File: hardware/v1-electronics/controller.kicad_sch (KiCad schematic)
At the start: 15 parts, among them J3 Female JST-SH, SW8 SW_Push, U1 MDBT50Q-1MV2

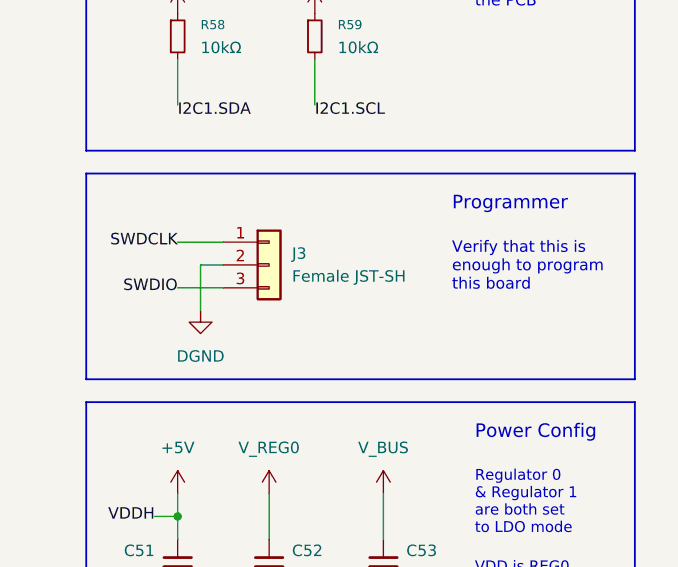
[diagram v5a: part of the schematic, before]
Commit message: feat(v1 hardware): aligned schematic symbols with pcb footprints
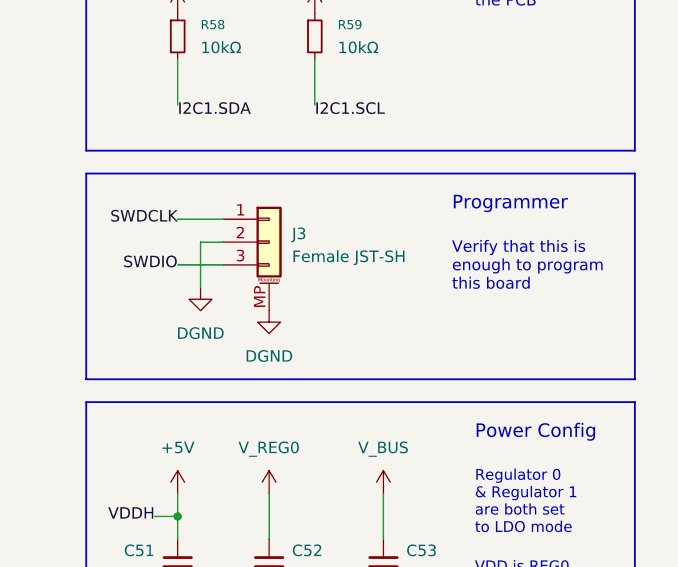
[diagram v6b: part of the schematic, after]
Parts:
- J3: symbol Connector_Generic:Conn_01x03 -> Connector_Generic_MountingPin:Conn_01x03_MountingPin
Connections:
- net DGND: now also J3.MP (MountPin)
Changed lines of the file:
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@@
 	(wire
 		(pts
-			(xy 25.4 76.2) (xy 30.48 76.2)
+			(xy 25.4 73.66) (xy 30.48 73.66)
 		)
 		(stroke
@@
 	(wire
 		(pts
-			(xy 27.94 78.74) (xy 27.94 73.66)
+			(xy 27.94 76.2) (xy 27.94 71.12)
 		)
 		(stroke
@@
 	(wire
 		(pts
-			(xy 27.94 73.66) (xy 30.48 73.66)
+			(xy 27.94 71.12) (xy 30.48 71.12)
 		)
 		(stroke
@@
 	(wire
 		(pts
-			(xy 25.4 71.12) (xy 30.48 71.12)
+			(xy 25.4 68.58) (xy 30.48 68.58)
 		)
 		(stroke
@@
 	)
 	(label "SWDCLK"
-		(at 25.4 71.12 180)
+		(at 25.4 68.58 180)
 		(effects
 			(font
@@
 	)
 	(label "SWDIO"
-		(at 25.4 76.2 180)
+		(at 25.4 73.66 180)
 		(effects
 			(font
@@
 	(symbol
 		(lib_id "power:GND")
-		(at 27.94 78.74 0)
+		(at 27.94 76.2 0)
 		(unit 1)
 		(body_style 1)
@@
 		(dnp no)
 		(property "Reference" "#PWR0123"
-			(at 27.94 85.09 0)
+			(at 27.94 82.55 0)
 			(hide yes)
 			(show_name no)
@@
 		)
 		(property "Value" "DGND"
-			(at 27.94 83.82 0)
+			(at 27.94 81.28 0)
 			(show_name no)
 			(do_not_autoplace no)
@@
 		)
 		(property "Footprint" ""
-			(at 27.94 78.74 0)
+			(at 27.94 76.2 0)
 			(hide yes)
 			(show_name no)
@@
 		)
 		(property "Datasheet" ""
-			(at 27.94 78.74 0)
+			(at 27.94 76.2 0)
 			(hide yes)
 			(show_name no)
@@
 		)
 		(property "Description" "Power symbol creates a global label with name \"GND\" , ground"
-			(at 27.94 78.74 0)
+			(at 27.94 76.2 0)
 			(hide yes)
 			(show_name no)
@@
 	)
 	(symbol
+		(lib_id "power:GND")
+		(at 35.56 78.74 0)
+		(unit 1)
+		(body_style 1)
+		(exclude_from_sim no)
+		(in_bom yes)
+		(on_board yes)
+		(in_pos_files yes)
+		(dnp no)
+		(property "Reference" "#PWR0156"
+			(at 35.56 85.09 0)
+			(hide yes)
+			(show_name no)
+			(do_not_autoplace no)
+			(effects
+				(font
+					(size 1.27 1.27)
+				)
+			)
+		)
+		(property "Value" "DGND"
+			(at 35.56 83.82 0)
+			(show_name no)
+			(do_not_autoplace no)
+			(effects
+				(font
+					(size 1.27 1.27)
+				)
+			)
+		)
+		(property "Footprint" ""
+			(at 35.56 78.74 0)
+			(hide yes)
+			(show_name no)
+			(do_not_autoplace no)
+			(effects
+				(font
+					(size 1.27 1.27)
+				)
+			)
+		)
+		(property "Datasheet" ""
+			(at 35.56 78.74 0)
+			(hide yes)
+			(show_name no)
+			(do_not_autoplace no)
+			(effects
+				(font
+					(size 1.27 1.27)
+				)
+			)
+		)
+		(property "Description" "Power symbol creates a global label with name \"GND\" , ground"
+			(at 35.56 78.74 0)
+			(hide yes)
+			(show_name no)
+			(do_not_autoplace no)
+			(effects
+				(font
+					(size 1.27 1.27)
+				)
+			)
+		)
+		(pin "1"
+		)
+		(instances
+			(project "slack"
+				(path "/504df67f-9f45-483f-90c8-f14c049b6b02/af928721-79e0-4dbd-9302-cd57a57ce5a4"
+					(reference "#PWR0156")
+					(unit 1)
+				)
+			)
+		)
+	)
+	(symbol
 		(lib_id "Device:R_Small")
 		(at 40.64 48.26 0)
@@
 	)
 	(symbol
-		(lib_id "Connector_Generic:Conn_01x03")
-		(at 35.56 73.66 0)
+		(lib_id "Connector_Generic_MountingPin:Conn_01x03_MountingPin")
+		(at 35.56 71.12 0)
 		(unit 1)
 		(body_style 1)
@@
 		(fields_autoplaced yes)
 		(property "Reference" "J3"
-			(at 38.1 72.3899 0)
+			(at 38.1 70.2055 0)
 			(show_name no)
 			(do_not_autoplace no)
@@
 		)
 		(property "Value" "Female JST-SH"
-			(at 38.1 74.9299 0)
+			(at 38.1 72.7455 0)
 			(show_name no)
 			(do_not_autoplace no)
@@
 		)
 		(property "Footprint" "Connector_JST:JST_SH_BM03B-SRSS-TB_1x03-1MP_P1.00mm_Vertical"
-			(at 35.56 73.66 0)
+			(at 35.56 71.12 0)
 			(hide yes)
 			(show_name no)
@@
 		)
 		(property "Datasheet" ""
-			(at 35.56 73.66 0)
+			(at 35.56 71.12 0)
 			(hide yes)
 			(show_name no)
@@
 			)
 		)
-		(property "Description" "Generic connector, single row, 01x03, script generated (kicad-library-utils/schlib/autogen/connector/)"
-			(at 35.56 73.66 0)
+		(property "Description" "Generic connectable mounting pin connector, single row, 01x03, script generated (kicad-library-utils/schlib/autogen/connector/)"
+			(at 35.56 71.12 0)
 			(hide yes)
 			(show_name no)
@@
 		)
 		(property "Availability" ""
-			(at 35.56 73.66 0)
+			(at 35.56 71.12 0)
 			(hide yes)
 			(show_name no)
@@
 		)
 		(property "CREATOR" ""
-			(at 35.56 73.66 0)
+			(at 35.56 71.12 0)
 			(hide yes)
 			(show_name no)
@@
 		)
 		(property "Check_prices" ""
-			(at 35.56 73.66 0)
+			(at 35.56 71.12 0)
 			(hide yes)
 			(show_name no)
@@
 		)
 		(property "MANUFACTURER" ""
-			(at 35.56 73.66 0)
+			(at 35.56 71.12 0)
 			(hide yes)
 			(show_name no)
@@
 		)
 		(property "MAXIMUM_PACKAGE_HEIGHT" ""
-			(at 35.56 73.66 0)
+			(at 35.56 71.12 0)
 			(hide yes)
 			(show_name no)
@@
 		)
 		(property "MF" ""
-			(at 35.56 73.66 0)
+			(at 35.56 71.12 0)
 			(hide yes)
 			(show_name no)
@@
 		)
 		(property "MP" ""
-			(at 35.56 73.66 0)
+			(at 35.56 71.12 0)
 			(hide yes)
 			(show_name no)
@@
 		)
 		(property "PARTREV" ""
-			(at 35.56 73.66 0)
+			(at 35.56 71.12 0)
 			(hide yes)
 			(show_name no)
@@
 		)
 		(property "Package" ""
-			(at 35.56 73.66 0)
+			(at 35.56 71.12 0)
 			(hide yes)
 			(show_name no)
@@
 		)
 		(property "Price" ""
-			(at 35.56 73.66 0)
+			(at 35.56 71.12 0)
 			(hide yes)
 			(show_name no)
@@
 		)
 		(property "SNAPEDA_PACKAGE_ID" ""
-			(at 35.56 73.66 0)
+			(at 35.56 71.12 0)
 			(hide yes)
 			(show_name no)
@@
 		)
 		(property "STANDARD" ""
-			(at 35.56 73.66 0)
+			(at 35.56 71.12 0)
 			(hide yes)
 			(show_name no)
@@
 		)
 		(property "SnapEDA_Link" ""
-			(at 35.56 73.66 0)
+			(at 35.56 71.12 0)
 			(hide yes)
 			(show_name no)
@@
 		)
 		(property "VERIFIER" ""
-			(at 35.56 73.66 0)
+			(at 35.56 71.12 0)
 			(hide yes)
 			(show_name no)
@@
 		(pin "2"
 		)
+		(pin "MP"
+		)
 		(instances
